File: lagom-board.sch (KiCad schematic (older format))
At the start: 0 parts

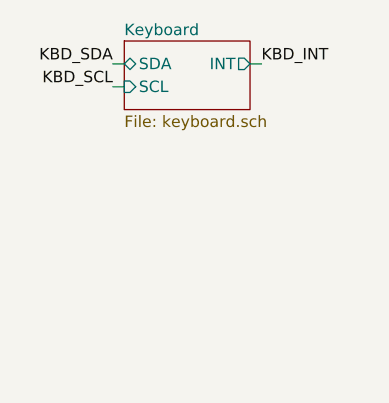
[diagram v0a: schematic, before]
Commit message: Added display, and keyboard reset pin
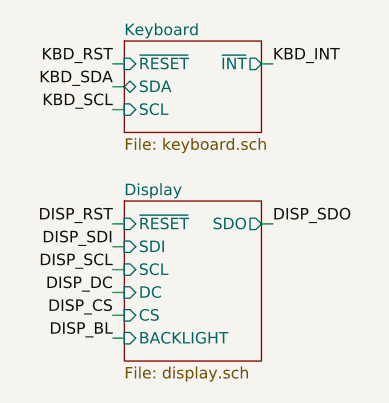
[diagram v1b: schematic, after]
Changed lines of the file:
@@
 $Descr A4 11693 8268
 encoding utf-8
-Sheet 1 2
+Sheet 1 3
 Title ""
 Date ""
@@
 $EndDescr
 $Sheet
-S 2500 3850 550  300
+S 2500 3850 600  400
 U 5C44BF88
 F0 "Keyboard" 50
 F1 "keyboard.sch" 50
-F2 "INT" O R 3050 3950 50
-F3 "SCL" I L 2500 4050 50
-F4 "SDA" B L 2500 3950 50
+F2 "SCL" I L 2500 4150 50
+F3 "SDA" B L 2500 4050 50
+F4 "~RESET~" I L 2500 3950 50
+F5 "~INT~" O R 3100 3950 50
 $EndSheet
 Wire Wire Line
-	3050 3950 3100 3950
-Wire Wire Line
-	2500 3950 2450 3950
+	3100 3950 3150 3950
 Wire Wire Line
 	2500 4050 2450 4050
-Text Label 3100 3950 0    50   ~ 0
+Wire Wire Line
+	2500 4150 2450 4150
+Text Label 3150 3950 0    50   ~ 0
 KBD_INT
+Text Label 2450 4050 2    50   ~ 0
+KBD_SDA
+Text Label 2450 4150 2    50   ~ 0
+KBD_SCL
+$Sheet
+S 2500 4550 600  700
+U 5C4E0551
+F0 "Display" 50
+F1 "display.sch" 50
+F2 "SDO" O R 3100 4650 50
+F3 "SDI" I L 2500 4750 50
+F4 "DC" I L 2500 4950 50
+F5 "SCL" I L 2500 4850 50
+F6 "CS" I L 2500 5050 50
+F7 "~RESET~" I L 2500 4650 50
+F8 "BACKLIGHT" I L 2500 5150 50
+$EndSheet
+Wire Wire Line
+	2500 4650 2450 4650
+Wire Wire Line
+	2500 4750 2450 4750
+Wire Wire Line
+	2500 4850 2450 4850
+Wire Wire Line
+	2500 4950 2450 4950
+Wire Wire Line
+	2500 5050 2450 5050
+Wire Wire Line
+	3100 4650 3150 4650
+Text Label 2450 4650 2    50   ~ 0
+DISP_RST
+Text Label 2450 4750 2    50   ~ 0
+DISP_SDI
+Text Label 2450 4850 2    50   ~ 0
+DISP_SCL
+Text Label 2450 4950 2    50   ~ 0
+DISP_DC
+Text Label 2450 5050 2    50   ~ 0
+DISP_CS
+Wire Wire Line
+	2450 3950 2500 3950
 Text Label 2450 3950 2    50   ~ 0
-KBD_SDA
-Text Label 2450 4050 2    50   ~ 0
-KBD_SCL
+KBD_RST
+Text Label 3150 4650 0    50   ~ 0
+DISP_SDO
+Wire Wire Line
+	2500 5150 2450 5150
+Text Label 2450 5150 2    50   ~ 0
+DISP_BL
 $EndSCHEMATC
